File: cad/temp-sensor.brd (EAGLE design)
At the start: 100 x 80 mm, 47 parts, among them Q1 300S14-U, Q2 320S14-U, Q3 320S14-U, U1 SE555D, U2 SE555D, U4 MCP6001UT-I/OT, U5 MCP6001UT-I/OT, U6 MCP6001UT-I/OT, U7 MCP6001UT-I/OT, U8 NCV4264-2CST50T3G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

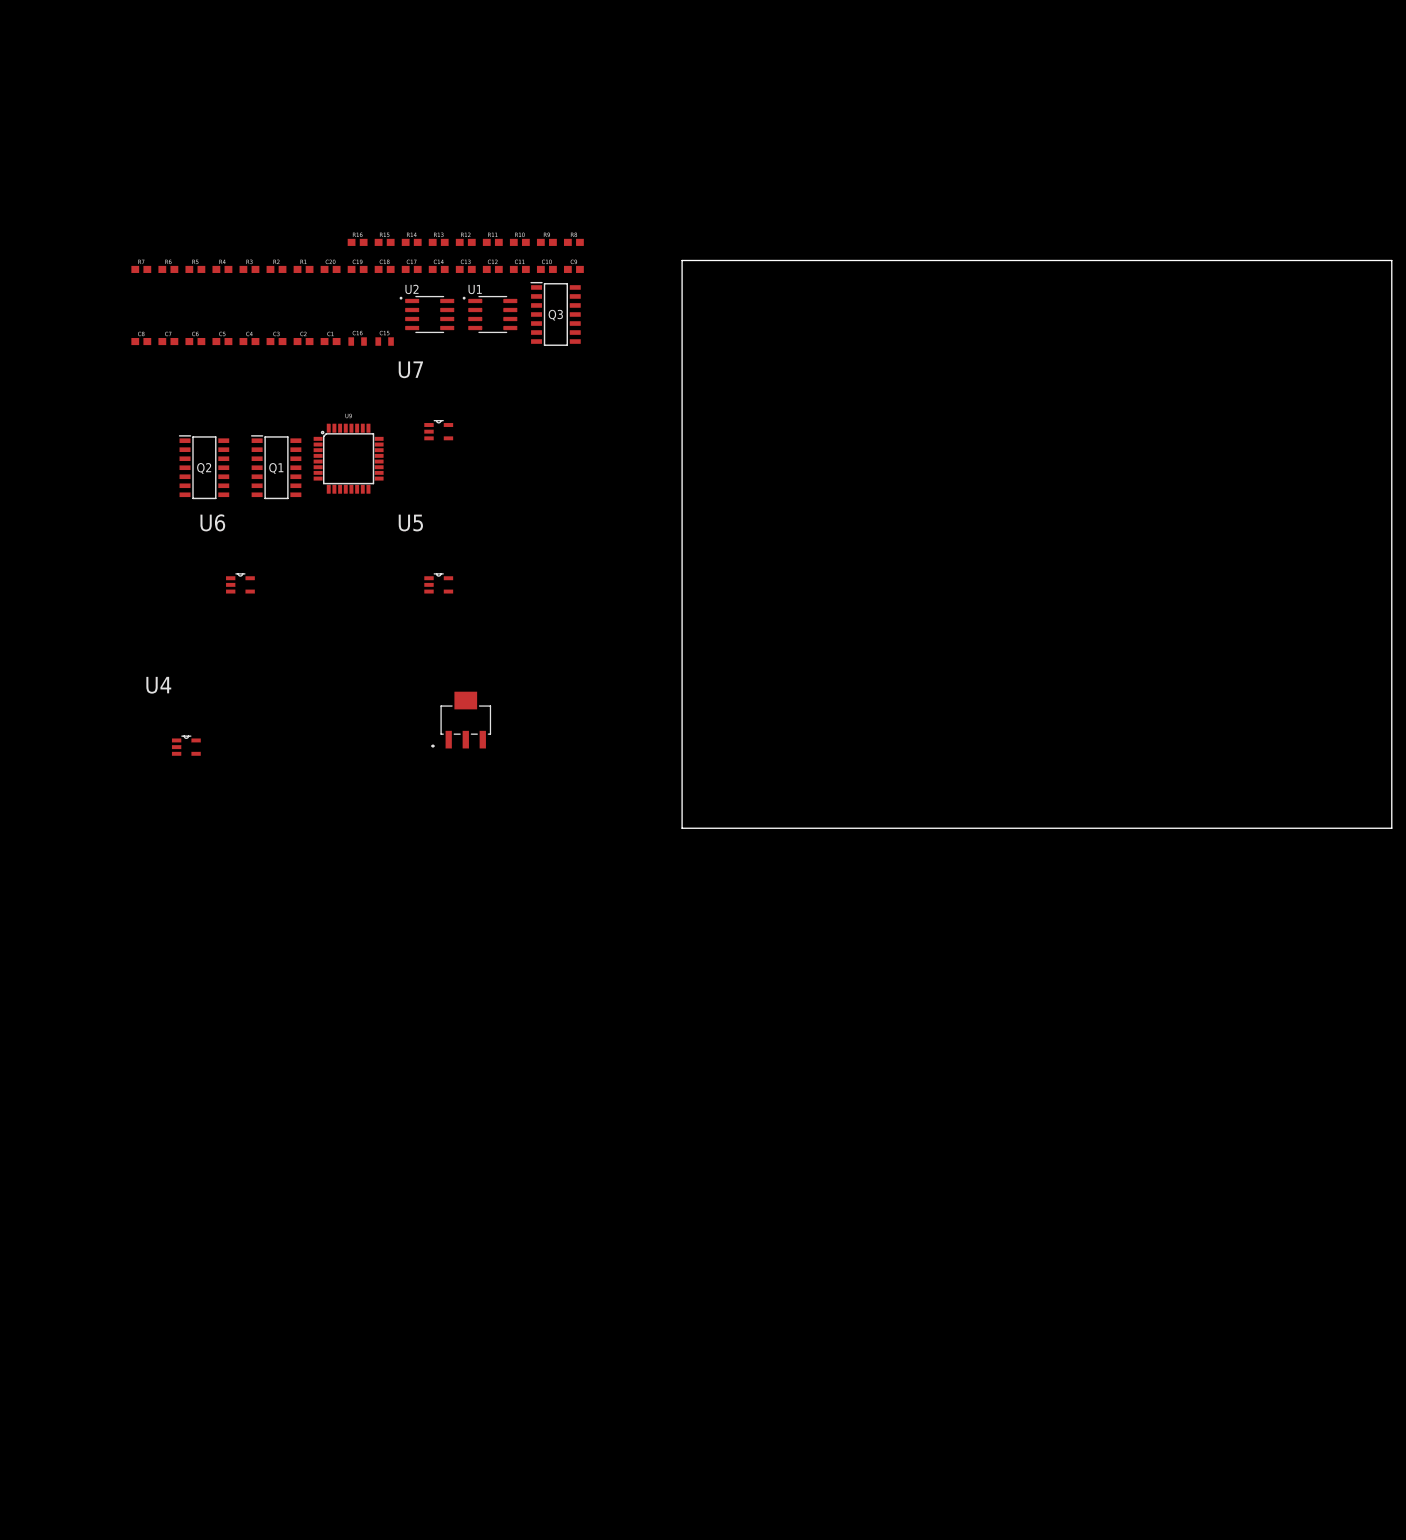
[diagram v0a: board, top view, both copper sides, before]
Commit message: Connect MCU
Add MCU connection to 555 timers, add correct bypass caps for opamps, add battery holder, add LEDs for PWR_ON/SCK signals, add 6-pin header for SPI programming + MCU reset
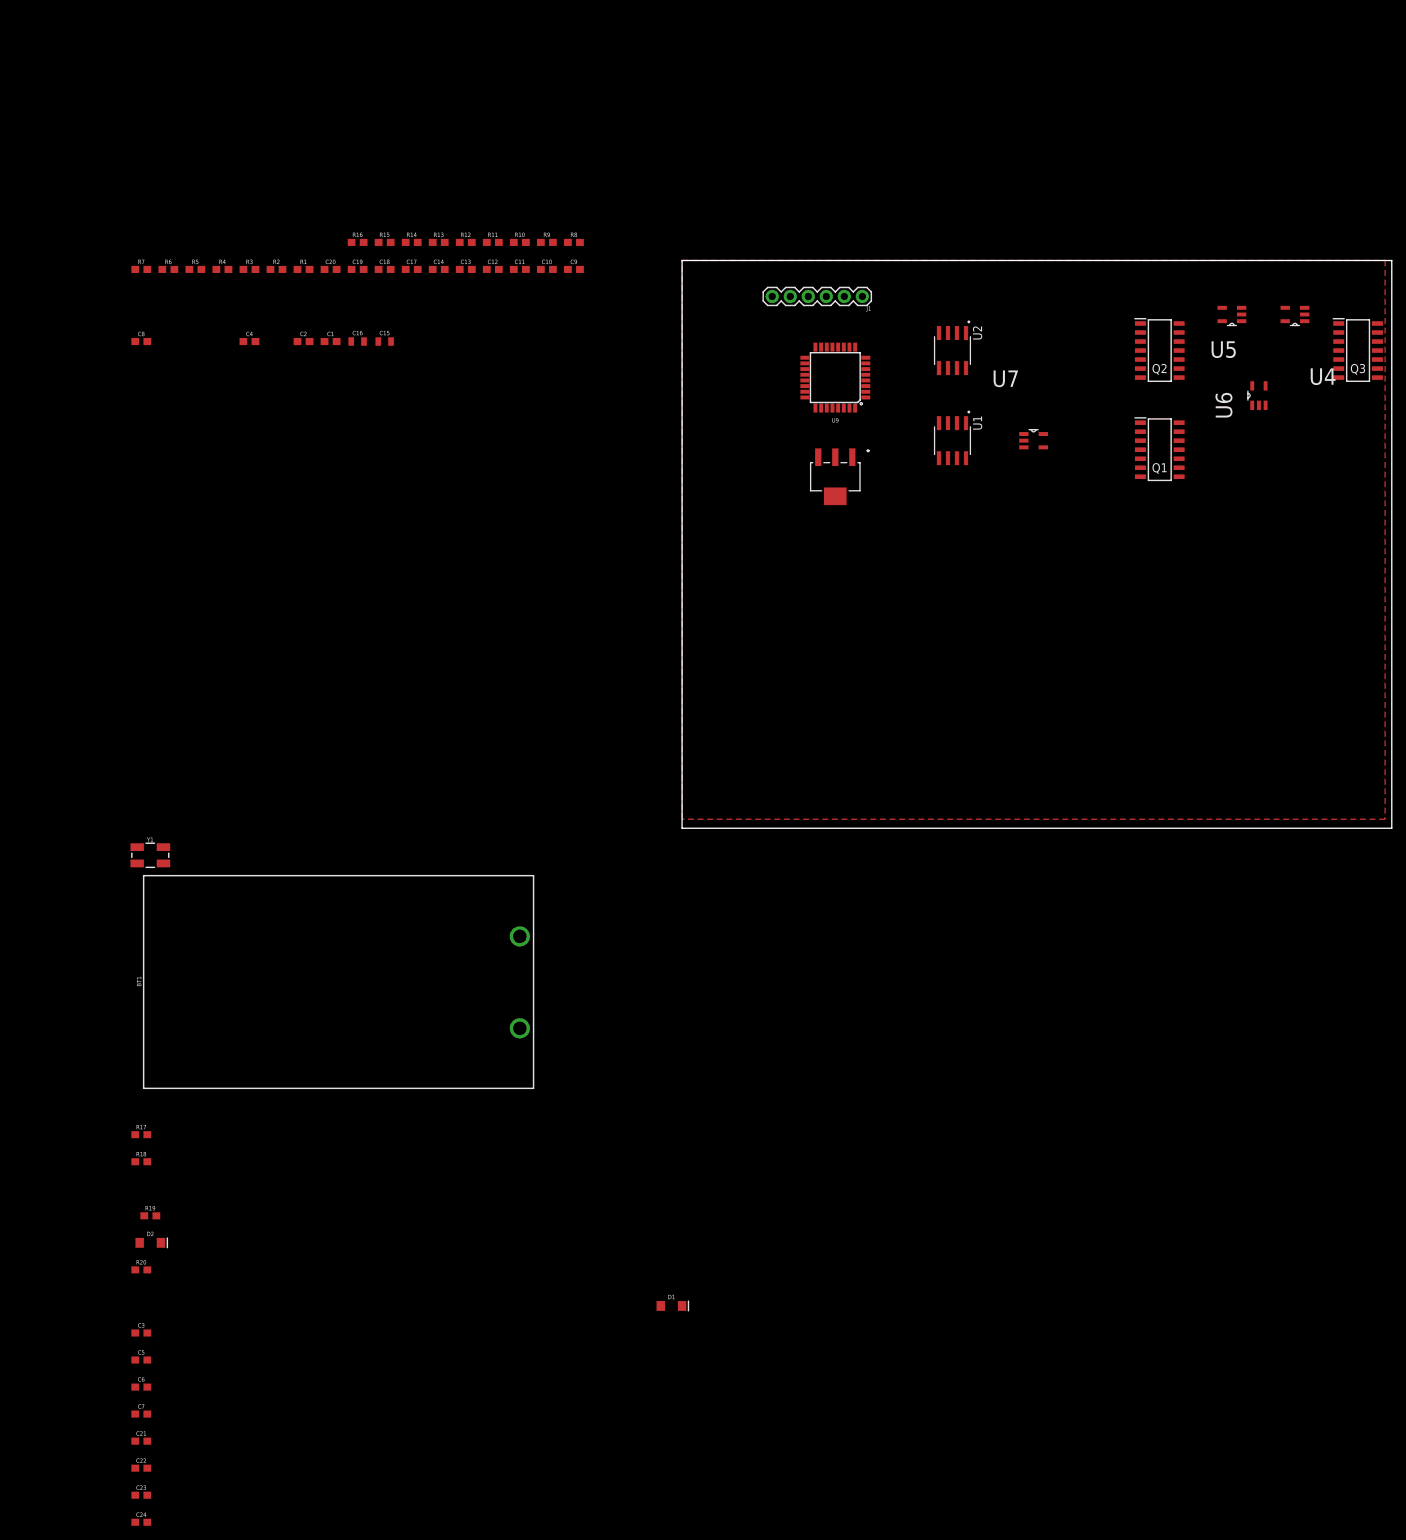
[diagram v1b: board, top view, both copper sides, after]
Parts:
- added BT1: (no value), SparkFun-Batteries:BATTCON_9V
- added C21, C22, C23, C24: 1.0uF, SparkFun-Capacitors:0603
- added D1, D2: GREEN, SparkFun-LED:LED-1206
- added J1: (no value), SparkFun-Connectors:1X06
- added R17, R18: 10k, SparkFun-Resistors:0603
- added R19, R20: 330, SparkFun-Resistors:0603
- added Y1: 16MHz, SparkFun-Clocks:CRYSTAL-SMD-5X3.2-4PAD
- C3, C5, C6, C7: value 0.1uF -> 10nF
- moved U4 167.7 mm to (86.4, 72.4), turned to 180 degrees
- moved C7 151.2 mm to (-76.2, -82.5)
- moved C6 147.5 mm to (-76.2, -78.7)
- moved U6 146.0 mm to (81.3, 61.0), turned to 90 degrees
- moved C5 144.0 mm to (-76.2, -74.9)
- moved C3 141.0 mm to (-76.2, -71.1)
- moved Q2 135.6 mm to (67.3, 67.3)
- moved Q1 124.5 mm to (67.3, 53.3)
- moved U5 118.1 mm to (77.5, 72.4), turned to 180 degrees
- moved Q3 113.1 mm to (95.2, 67.3)
- moved U7 83.8 mm to (49.5, 54.6)
- moved U2 73.8 mm to (38.1, 67.3), turned to 270 degrees
- moved U9 69.5 mm to (21.6, 63.5), turned to 180 degrees
- moved U1 67.2 mm to (38.1, 54.6), turned to 270 degrees
- moved U8 62.3 mm to (21.6, 49.5), turned to 180 degrees
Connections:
- net N$6 renamed FREQ_CTRL
- removed net N$4: C19.2, U9.7
- removed net N$5: C20.2, U9.8
- removed net N$7: U1.4
- removed net N$8: U1.7
- removed net N$9: U2.4
- new net 555_RST_N: R17.1, R18.1, U1.4, U2.4, U9.23
- new net N$1: C17.1
- new net N$2: D1.A, R19.1
- new net N$3: D2.A, R20.1
- new net XTAL1: C19.2, U9.7, Y1.1
- new net XTAL2: C20.2, U9.8, Y1.3
- net +5V: now also C21.1, C22.1, C23.1, C24.1, J1.1, R17.2, R18.2, R20.2; no longer C17.1
- net +9V: now also BT1.+
- net CIPO: now also J1.4
- net COPI: now also J1.3
- net FREQ_OUT: now also U9.9
- net GND: now also BT1.-, C21.2, C22.2, C23.2, C24.2, D1.C, D2.C, J1.6
- net MCU_RST: now also J1.2
- net PULSE_OUT: now also U9.32
- net PULSE_THRES: now also U1.7
- net SCK: now also J1.5, R19.2
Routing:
- added copper zone on layer 1, net GND

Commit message: Initialize layout file
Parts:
- added J2: (no value), SparkFun-Connectors:1X02
- added R21, R24: 10k, SparkFun-Resistors:0603
- added S1: MOMENTARY-SWITCH-SPST-PTH-6.0MM, SparkFun-Switches:TACTILE_SWITCH_PTH_6.0MM
- R18: value 10k -> 43k
- moved C24 207.3 mm to (-87.6, 109.2)
- moved C23 203.3 mm to (-83.8, 109.2)
- moved C22 199.4 mm to (-80.0, 109.2)
- moved C7 197.1 mm to (-30.5, 109.2)
- moved C21 195.6 mm to (-76.2, 109.2)
- moved C6 194.4 mm to (-26.7, 109.2)
- moved C5 191.7 mm to (-22.9, 109.2)
- moved C3 190.4 mm to (-15.2, 109.2)
- moved R18 185.8 mm to (92.7, 30.5)
- moved D1 180.8 mm to (-72.4, 99.1)
- moved R20 175.4 mm to (-83.8, 113.0)
- moved R19 167.7 mm to (-80.0, 113.0)
- moved D2 157.5 mm to (-77.5, 99.1)
- moved R17 156.3 mm to (-72.4, 113.0)
- moved R3 146.6 mm to (77.5, 30.5)
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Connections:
- new net PBTN: R24.1, S1.3, U9.24
- new net PULSE_TRIG: R21.1, U1.2, U9.11
- new net START_C: Q3.14, Q3.9, R18.1
- net +5V: now also Q3.10, Q3.12, R21.2, R24.2; no longer R18.2
- net 555_RST_N: no longer R18.1
- net GND: now also R18.2, S1.1
- net PTAT_BASE: now also Q3.13
- net SCL: now also J2.2
- net SDA: now also J2.1
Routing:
- removed copper zone on layer 1, net GND

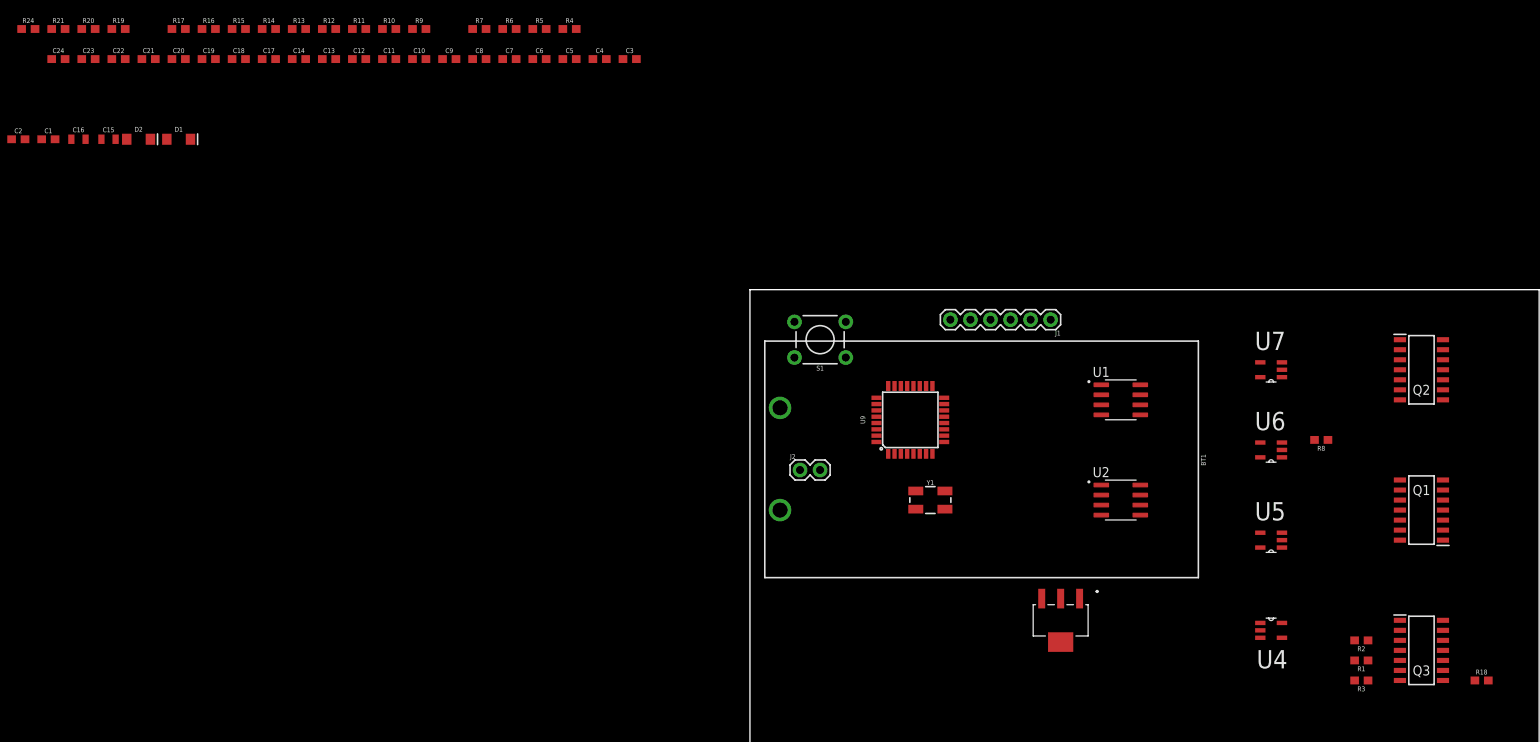
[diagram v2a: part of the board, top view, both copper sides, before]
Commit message: Add placement and passives
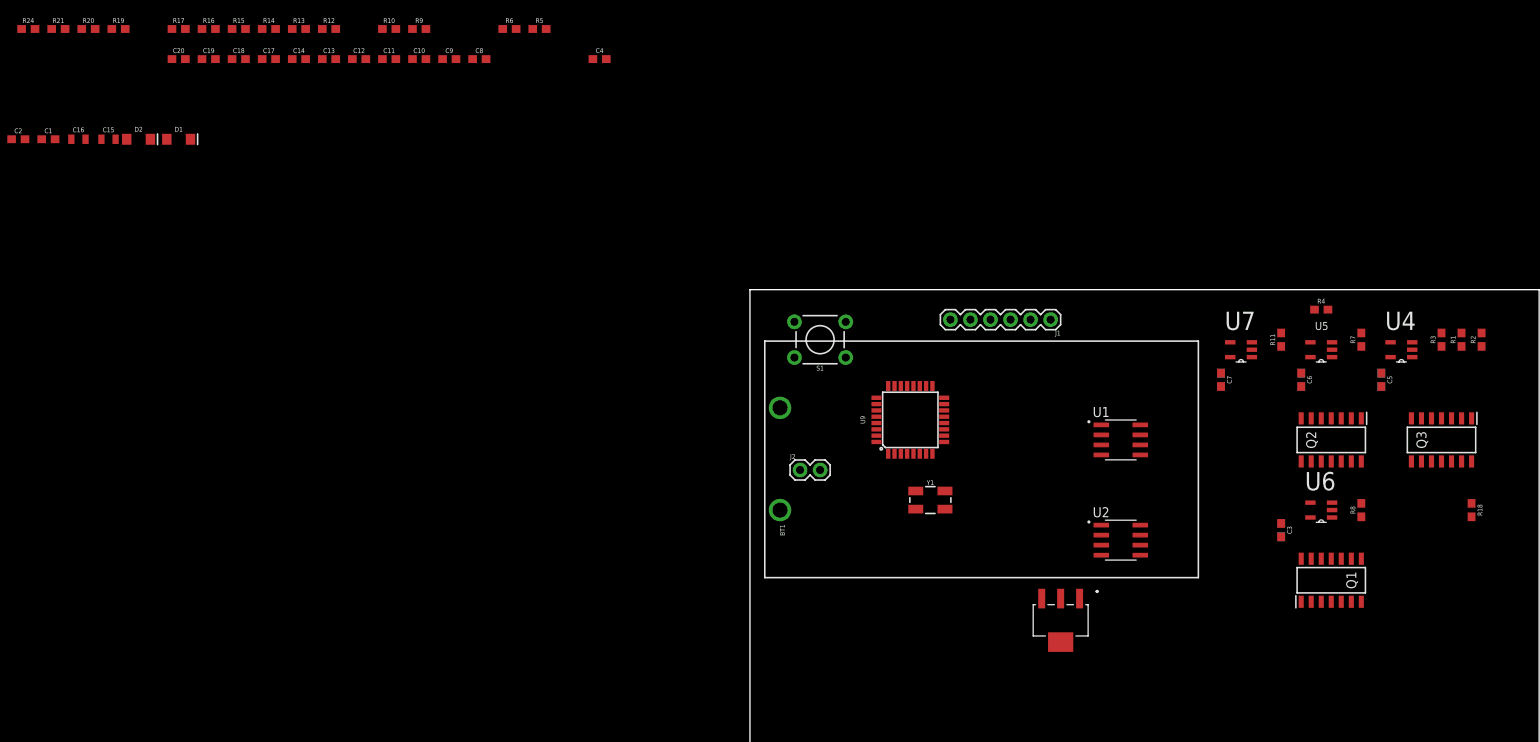
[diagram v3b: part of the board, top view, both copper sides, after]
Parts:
- moved C24 166.0 mm to (67.3, 49.5), flipped to the bottom, turned to 270 degrees
- moved C21 161.4 mm to (80.0, 68.6), flipped to the bottom, turned to 270 degrees
- moved C22 155.3 mm to (69.8, 68.6), flipped to the bottom, turned to 270 degrees
- moved C23 149.2 mm to (59.7, 68.6), flipped to the bottom, turned to 270 degrees
- moved R11 123.3 mm to (67.3, 73.7), turned to 270 degrees
- moved R7 118.5 mm to (77.5, 73.7), turned to 270 degrees
- moved C5 110.6 mm to (80.0, 68.6), turned to 270 degrees
- moved C6 104.7 mm to (69.8, 68.6), turned to 270 degrees
- moved C3 101.9 mm to (67.3, 49.5), turned to 270 degrees
- moved R4 101.7 mm to (72.4, 77.5)
- moved C7 98.9 mm to (59.7, 68.6), turned to 270 degrees
- moved R3 44.4 mm to (87.6, 73.7), turned to 270 degrees
- moved R1 42.6 mm to (90.2, 73.7), turned to 90 degrees
- moved R2 41.0 mm to (92.7, 73.7), turned to 90 degrees
- moved U4 39.2 mm to (82.5, 72.4), turned to 180 degrees
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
